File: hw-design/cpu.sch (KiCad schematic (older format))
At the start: 15 parts, among them P2 HEADER_5X2, P3 HEADER_5X2, U1 LPC1113FBD48/302, X1 10MHz

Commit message: ERC passing
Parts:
- removed P2, P3: HEADER_5X2, MOD_Footprints_Lib:PIN_ARRAY_5x2, symbol CONN_5X2
- added P1, P2: CONN_02X05, symbol CONN_02X05
- renumbered C10 to C13, C11 to C14, C14 to C15, C13 to C16, R21 to R23, R15 to R24, R29 to R25, R30 to R26, R26 to R27, R27 to R28, U1 to U4
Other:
- moved on the sheet: R27, R28

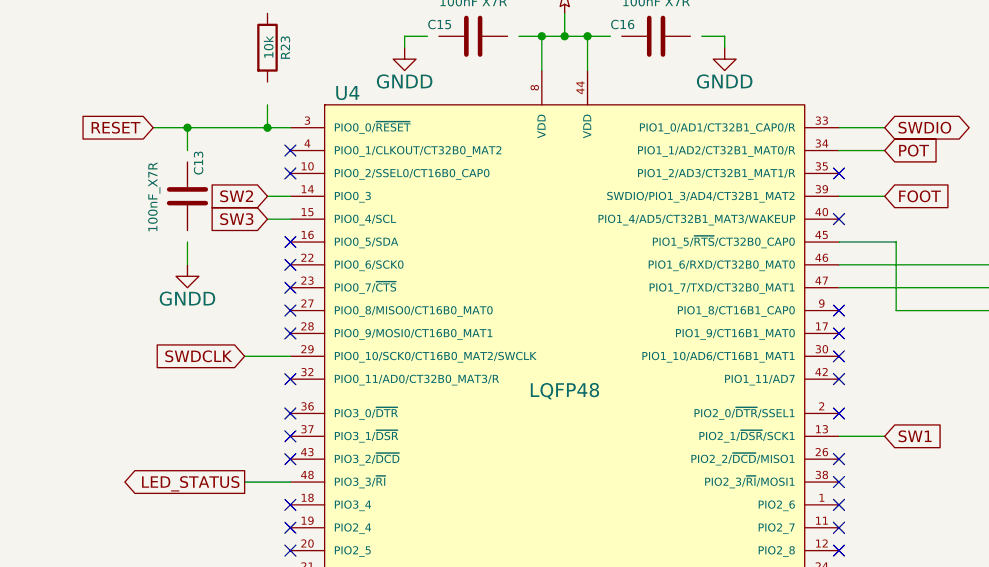
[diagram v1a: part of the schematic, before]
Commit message: wip: footprint association using default kicad libraries
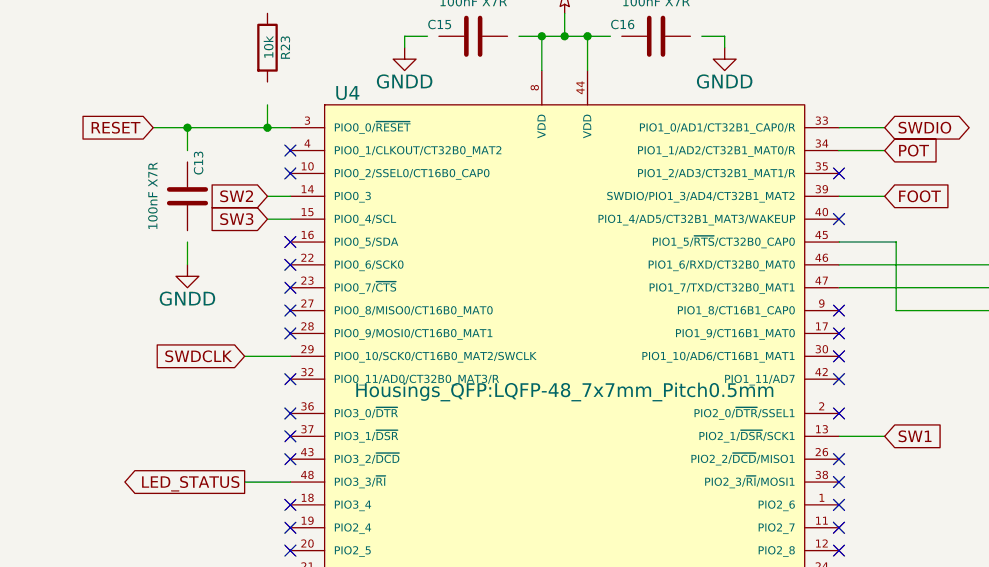
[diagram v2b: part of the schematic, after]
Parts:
- C12, C14, C15, C16: footprint MOD_Footprints_Lib:SM0603 -> Capacitors_SMD:C_0603
- C13: value 100nF_X7R -> 100nF X7R; footprint MOD_Footprints_Lib:SM0603 -> Capacitors_SMD:C_0603
- P1, P2: footprint (none) -> Pin_Headers:Pin_Header_Straight_2x05
- R23, R24, R25, R26, R27, R28: footprint MOD_Footprints_Lib:SM0603 -> Resistors_SMD:R_0603
- U4: footprint LQFP48 -> Housings_QFP:LQFP-48_7x7mm_Pitch0.5mm
- X1: footprint MOD_Footprints_Lib:HC_49US -> Crystals_Oscillators_SMD:Q_49U3HMS
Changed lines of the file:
@@
 F 0 "C15" V 4000 1750 40  0000 L CNN
 F 1 "100nF X7R" V 3900 1800 40  0000 L CNN
-F 2 "MOD_Footprints_Lib:SM0603" H 4088 1800 30  0001 C CNN
+F 2 "Capacitors_SMD:C_0603" H 4088 1800 30  0001 C CNN
 F 3 "~" H 4050 1950 60  0000 C CNN
 	1    4050 1950
@@
 F 0 "C16" V 4900 1750 40  0000 L CNN
 F 1 "100nF X7R" V 5000 1800 40  0000 L CNN
-F 2 "MOD_Footprints_Lib:SM0603" H 4888 1800 30  0001 C CNN
+F 2 "Capacitors_SMD:C_0603" H 4888 1800 30  0001 C CNN
 F 3 "~" H 4850 1950 60  0000 C CNN
 	1    4850 1950
@@
 F 0 "X1" H 2700 4800 60  0000 C CNN
 F 1 "10MHz" H 2700 4550 60  0000 C CNN
-F 2 "MOD_Footprints_Lib:HC_49US" H 2700 4700 60  0001 C CNN
+F 2 "Crystals_Oscillators_SMD:Q_49U3HMS" H 2700 4700 60  0001 C CNN
 F 3 "~" H 2700 4700 60  0000 C CNN
 	1    2700 4700
@@
 F 0 "C14" V 2950 5000 40  0000 L CNN
 F 1 "18pF X7R" V 3250 4900 40  0000 L CNN
-F 2 "MOD_Footprints_Lib:SM0603" H 3138 4900 30  0001 C CNN
+F 2 "Capacitors_SMD:C_0603" H 3138 4900 30  0001 C CNN
 F 3 "~" H 3100 5050 60  0000 C CNN
 	1    3100 5050
@@
 F 0 "C12" V 2100 5000 40  0000 L CNN
 F 1 "18pF X7R" V 2400 4900 40  0000 L CNN
-F 2 "MOD_Footprints_Lib:SM0603" H 2288 4900 30  0001 C CNN
+F 2 "Capacitors_SMD:C_0603" H 2288 4900 30  0001 C CNN
 F 3 "~" H 2250 5050 60  0000 C CNN
 	1    2250 5050
@@
 F 0 "R23" V 3230 2000 40  0000 C CNN
 F 1 "10k" V 3157 2001 40  0000 C CNN
-F 2 "MOD_Footprints_Lib:SM0603" V 3080 2000 30  0001 C CNN
+F 2 "Resistors_SMD:R_0603" V 3080 2000 30  0001 C CNN
 F 3 "~" H 3150 2000 30  0000 C CNN
 	1    3150 2000
@@
 P 2800 2650
 F 0 "C13" V 2850 2450 40  0000 L CNN
-F 1 "100nF_X7R" V 2650 2500 40  0000 L CNN
-F 2 "MOD_Footprints_Lib:SM0603" H 2838 2500 30  0001 C CNN
+F 1 "100nF X7R" V 2650 2500 40  0000 L CNN
+F 2 "Capacitors_SMD:C_0603" H 2838 2500 30  0001 C CNN
 F 3 "~" H 2800 2650 60  0000 C CNN
 	1    2800 2650
@@
 F 0 "R28" V 9100 4850 40  0000 C CNN
 F 1 "100R" V 9007 4851 40  0000 C CNN
-F 2 "MOD_Footprints_Lib:SM0603" V 8930 4850 30  0001 C CNN
+F 2 "Resistors_SMD:R_0603" V 8930 4850 30  0001 C CNN
 F 3 "~" H 9000 4850 30  0000 C CNN
 	1    9000 4850
@@
 F 0 "R27" V 8900 4750 40  0000 C CNN
 F 1 "100R" V 9007 4751 40  0000 C CNN
-F 2 "MOD_Footprints_Lib:SM0603" V 8930 4750 30  0001 C CNN
+F 2 "Resistors_SMD:R_0603" V 8930 4750 30  0001 C CNN
 F 3 "~" H 9000 4750 30  0000 C CNN
 	1    9000 4750
@@
 F 0 "U4" H 3500 4800 60  0000 C CNN
 F 1 "LPC1113FBD48/302" H 5100 2150 60  0000 C CNN
-F 2 "LQFP48" H 4450 3500 60  0000 C CNN
+F 2 "Housings_QFP:LQFP-48_7x7mm_Pitch0.5mm" H 4450 3500 60  0000 C CNN
 F 3 "" H 4450 3500 60  0000 C CNN
 	1    4450 3500
@@
 F 0 "R24" V 7180 3450 40  0000 C CNN
 F 1 "0R" V 7107 3451 40  0000 C CNN
-F 2 "MOD_Footprints_Lib:SM0603" V 7030 3450 30  0001 C CNN
+F 2 "Resistors_SMD:R_0603" V 7030 3450 30  0001 C CNN
 F 3 "~" H 7100 3450 30  0000 C CNN
 	1    7100 3450
@@
 F 0 "R25" V 7180 3650 40  0000 C CNN
 F 1 "0R" V 7107 3651 40  0000 C CNN
-F 2 "MOD_Footprints_Lib:SM0603" V 7030 3650 30  0001 C CNN
+F 2 "Resistors_SMD:R_0603" V 7030 3650 30  0001 C CNN
 F 3 "~" H 7100 3650 30  0000 C CNN
 	1    7100 3650
@@
 F 0 "R26" V 7180 3850 40  0000 C CNN
 F 1 "0R" V 7107 3851 40  0000 C CNN
-F 2 "MOD_Footprints_Lib:SM0603" V 7030 3850 30  0001 C CNN
+F 2 "Resistors_SMD:R_0603" V 7030 3850 30  0001 C CNN
 F 3 "~" H 7100 3850 30  0000 C CNN
 	1    7100 3850
@@
 F 0 "P1" H 7100 3250 50  0000 C CNN
 F 1 "CONN_02X05" H 7100 2650 50  0000 C CNN
-F 2 "" H 7100 1750 60  0000 C CNN
+F 2 "Pin_Headers:Pin_Header_Straight_2x05" H 7100 1750 60  0001 C CNN
 F 3 "" H 7100 1750 60  0000 C CNN
 	1    7100 2950
@@
 F 0 "P2" H 8400 5250 50  0000 C CNN
 F 1 "CONN_02X05" H 8400 4650 50  0000 C CNN
-F 2 "" H 8400 3750 60  0000 C CNN
+F 2 "Pin_Headers:Pin_Header_Straight_2x05" H 8400 3750 60  0001 C CNN
 F 3 "" H 8400 3750 60  0000 C CNN
 	1    8400 4950

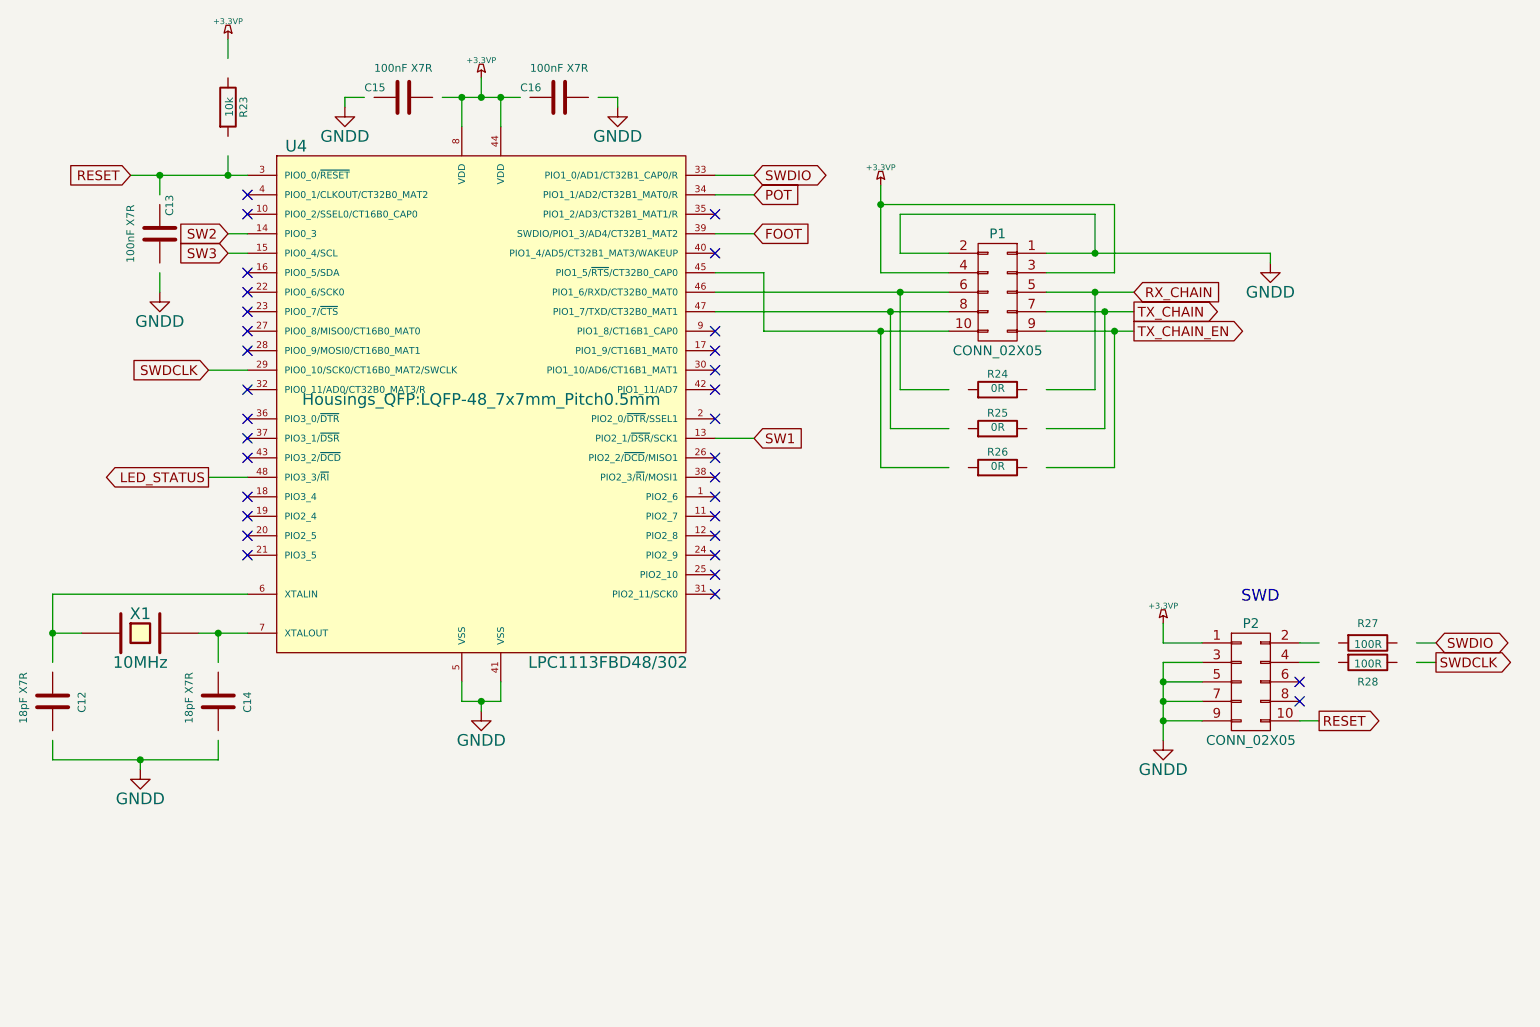
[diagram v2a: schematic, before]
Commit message: adding official kicad library as submodule
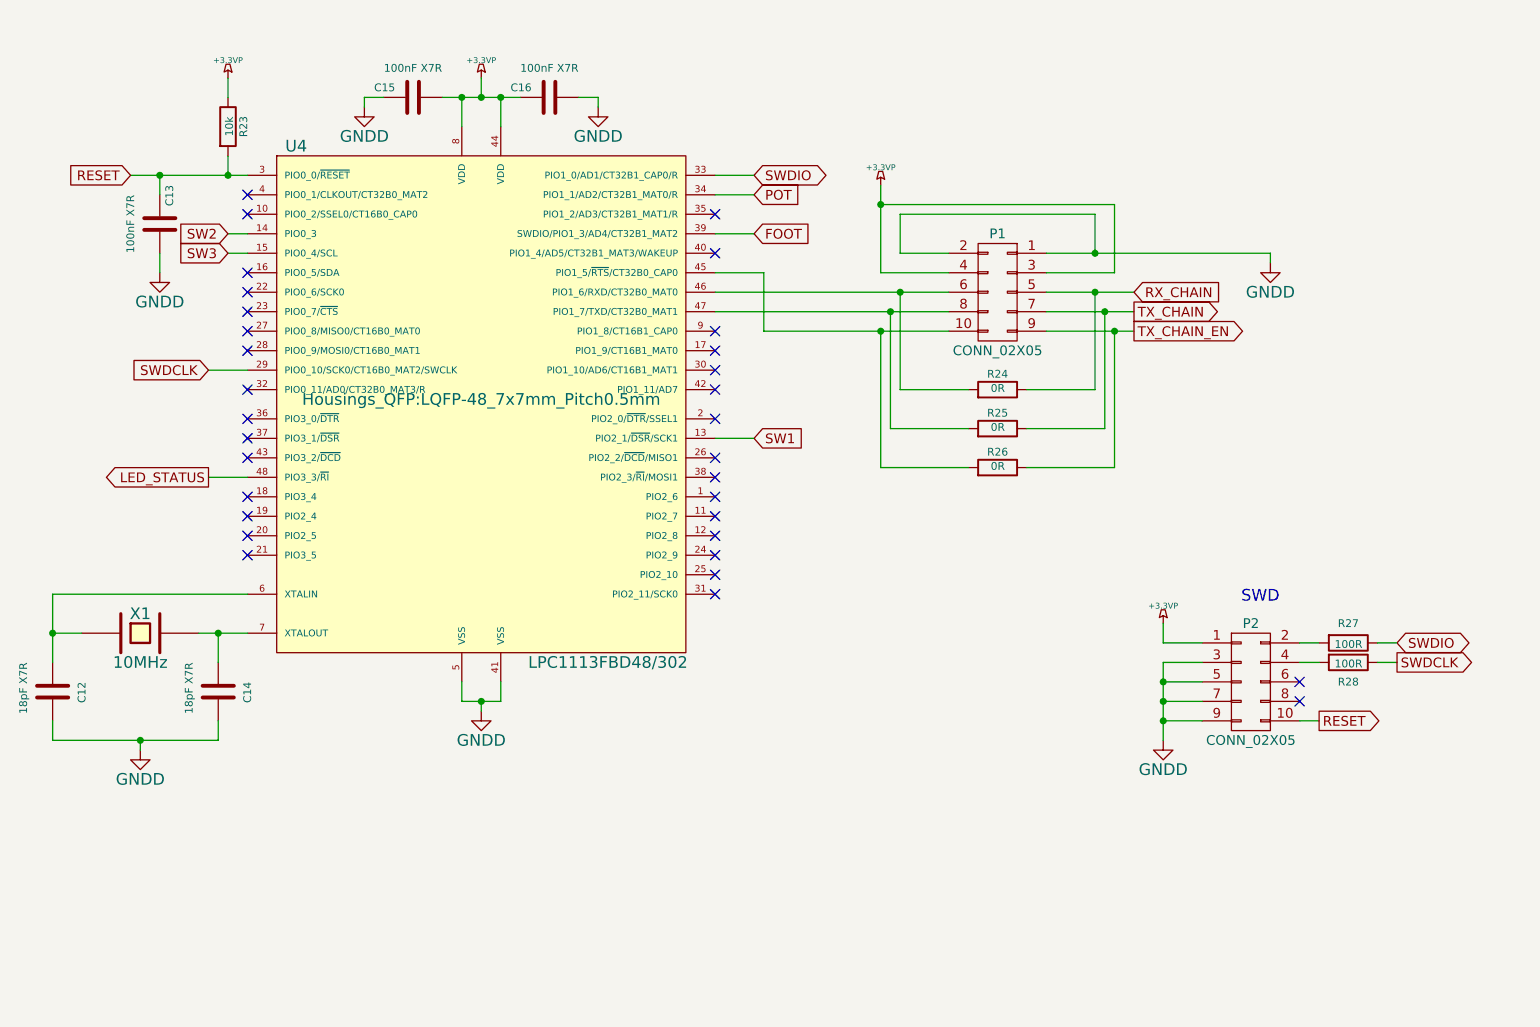
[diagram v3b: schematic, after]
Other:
- moved on the sheet: C12, C13, C14, C15, C16, R23, R27, R28
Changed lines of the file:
@@
 L C C15
 U 1 1 548B6D77
-P 4050 1950
-F 0 "C15" V 4000 1750 40  0000 L CNN
-F 1 "100nF X7R" V 3900 1800 40  0000 L CNN
-F 2 "Capacitors_SMD:C_0603" H 4088 1800 30  0001 C CNN
-F 3 "~" H 4050 1950 60  0000 C CNN
-	1    4050 1950
+P 4100 1950
+F 0 "C15" V 4050 1750 40  0000 L CNN
+F 1 "100nF X7R" V 3950 1800 40  0000 L CNN
+F 2 "Capacitors_SMD:C_0603" H 4138 1800 30  0001 C CNN
+F 3 "~" H 4100 1950 60  0000 C CNN
+	1    4100 1950
 	0    1    1    0
 $EndComp
@@
 L C C16
 U 1 1 548B6D84
-P 4850 1950
-F 0 "C16" V 4900 1750 40  0000 L CNN
-F 1 "100nF X7R" V 5000 1800 40  0000 L CNN
-F 2 "Capacitors_SMD:C_0603" H 4888 1800 30  0001 C CNN
-F 3 "~" H 4850 1950 60  0000 C CNN
-	1    4850 1950
+P 4800 1950
+F 0 "C16" V 4850 1750 40  0000 L CNN
+F 1 "100nF X7R" V 4950 1800 40  0000 L CNN
+F 2 "Capacitors_SMD:C_0603" H 4838 1800 30  0001 C CNN
+F 3 "~" H 4800 1950 60  0000 C CNN
+	1    4800 1950
 	0    1    -1   0
 $EndComp
@@
 L C C14
 U 1 1 548B6DA4
-P 3100 5050
-F 0 "C14" V 2950 5000 40  0000 L CNN
-F 1 "18pF X7R" V 3250 4900 40  0000 L CNN
-F 2 "Capacitors_SMD:C_0603" H 3138 4900 30  0001 C CNN
-F 3 "~" H 3100 5050 60  0000 C CNN
-	1    3100 5050
+P 3100 5000
+F 0 "C14" V 2950 4950 40  0000 L CNN
+F 1 "18pF X7R" V 3250 4850 40  0000 L CNN
+F 2 "Capacitors_SMD:C_0603" H 3138 4850 30  0001 C CNN
+F 3 "~" H 3100 5000 60  0000 C CNN
+	1    3100 5000
 	-1   0    0    1
 $EndComp
@@
 L C C12
 U 1 1 548B6DB7
-P 2250 5050
-F 0 "C12" V 2100 5000 40  0000 L CNN
-F 1 "18pF X7R" V 2400 4900 40  0000 L CNN
-F 2 "Capacitors_SMD:C_0603" H 2288 4900 30  0001 C CNN
-F 3 "~" H 2250 5050 60  0000 C CNN
-	1    2250 5050
+P 2250 5000
+F 0 "C12" V 2100 4950 40  0000 L CNN
+F 1 "18pF X7R" V 2400 4850 40  0000 L CNN
+F 2 "Capacitors_SMD:C_0603" H 2288 4850 30  0001 C CNN
+F 3 "~" H 2250 5000 60  0000 C CNN
+	1    2250 5000
 	-1   0    0    1
 $EndComp
@@
 L R R23
 U 1 1 548B6DBE
-P 3150 2000
-F 0 "R23" V 3230 2000 40  0000 C CNN
-F 1 "10k" V 3157 2001 40  0000 C CNN
-F 2 "Resistors_SMD:R_0603" V 3080 2000 30  0001 C CNN
-F 3 "~" H 3150 2000 30  0000 C CNN
-	1    3150 2000
+P 3150 2100
+F 0 "R23" V 3230 2100 40  0000 C CNN
+F 1 "10k" V 3157 2101 40  0000 C CNN
+F 2 "Resistors_SMD:R_0603" V 3080 2100 30  0001 C CNN
+F 3 "~" H 3150 2100 30  0000 C CNN
+	1    3150 2100
 	1    0    0    -1
 $EndComp
@@
 L C C13
 U 1 1 548B6DC5
-P 2800 2650
-F 0 "C13" V 2850 2450 40  0000 L CNN
-F 1 "100nF X7R" V 2650 2500 40  0000 L CNN
-F 2 "Capacitors_SMD:C_0603" H 2838 2500 30  0001 C CNN
-F 3 "~" H 2800 2650 60  0000 C CNN
-	1    2800 2650
+P 2800 2600
+F 0 "C13" V 2850 2400 40  0000 L CNN
+F 1 "100nF X7R" V 2650 2450 40  0000 L CNN
+F 2 "Capacitors_SMD:C_0603" H 2838 2450 30  0001 C CNN
+F 3 "~" H 2800 2600 60  0000 C CNN
+	1    2800 2600
 	1    0    0    1
 $EndComp
-Text GLabel 9350 4750 2    50   BiDi ~ 0
+Text GLabel 9150 4750 2    50   BiDi ~ 0
 SWDIO
-Text GLabel 9350 4850 2    50   Output ~ 0
+Text GLabel 9150 4850 2    50   Output ~ 0
 SWDCLK
 Text GLabel 5850 2350 2    50   BiDi ~ 0
@@
 L R R28
 U 1 1 548B6E40
-P 9000 4850
-F 0 "R28" V 9100 4850 40  0000 C CNN
-F 1 "100R" V 9007 4851 40  0000 C CNN
-F 2 "Resistors_SMD:R_0603" V 8930 4850 30  0001 C CNN
-F 3 "~" H 9000 4850 30  0000 C CNN
-	1    9000 4850
+P 8900 4850
+F 0 "R28" V 9000 4850 40  0000 C CNN
+F 1 "100R" V 8907 4851 40  0000 C CNN
+F 2 "Resistors_SMD:R_0603" V 8830 4850 30  0001 C CNN
+F 3 "~" H 8900 4850 30  0000 C CNN
+	1    8900 4850
 	0    1    1    0
 $EndComp
@@
 L R R27
 U 1 1 548B6E47
-P 9000 4750
-F 0 "R27" V 8900 4750 40  0000 C CNN
-F 1 "100R" V 9007 4751 40  0000 C CNN
-F 2 "Resistors_SMD:R_0603" V 8930 4750 30  0001 C CNN
-F 3 "~" H 9000 4750 30  0000 C CNN
-	1    9000 4750
+P 8900 4750
+F 0 "R27" V 8800 4750 40  0000 C CNN
+F 1 "100R" V 8907 4751 40  0000 C CNN
+F 2 "Resistors_SMD:R_0603" V 8830 4750 30  0001 C CNN
+F 3 "~" H 8900 4750 30  0000 C CNN
+	1    8900 4750
 	0    1    1    0
 $EndComp
@@
 L GNDD #PWR050
 U 1 1 54E37CE9
-P 2700 5400
-F 0 "#PWR050" H 2700 5150 60  0001 C CNN
-F 1 "GNDD" H 2700 5250 60  0000 C CNN
-F 2 "" H 2700 5400 60  0000 C CNN
-F 3 "" H 2700 5400 60  0000 C CNN
-	1    2700 5400
+P 2700 5300
+F 0 "#PWR050" H 2700 5050 60  0001 C CNN
+F 1 "GNDD" H 2700 5150 60  0000 C CNN
+F 2 "" H 2700 5300 60  0000 C CNN
+F 3 "" H 2700 5300 60  0000 C CNN
+	1    2700 5300
 	1    0    0    -1
 $EndComp
@@
 L GNDD #PWR051
 U 1 1 54E3D56C
-P 3750 2000
-F 0 "#PWR051" H 3750 1750 60  0001 C CNN
-F 1 "GNDD" H 3750 1850 60  0000 C CNN
-F 2 "" H 3750 2000 60  0000 C CNN
-F 3 "" H 3750 2000 60  0000 C CNN
-	1    3750 2000
+P 3850 2000
+F 0 "#PWR051" H 3850 1750 60  0001 C CNN
+F 1 "GNDD" H 3850 1850 60  0000 C CNN
+F 2 "" H 3850 2000 60  0000 C CNN
+F 3 "" H 3850 2000 60  0000 C CNN
+	1    3850 2000
 	1    0    0    -1
 $EndComp
@@
 L GNDD #PWR052
 U 1 1 54E3D638
-P 5150 2000
-F 0 "#PWR052" H 5150 1750 60  0001 C CNN
-F 1 "GNDD" H 5150 1850 60  0000 C CNN
-F 2 "" H 5150 2000 60  0000 C CNN
-F 3 "" H 5150 2000 60  0000 C CNN
-	1    5150 2000
+P 5050 2000
+F 0 "#PWR052" H 5050 1750 60  0001 C CNN
+F 1 "GNDD" H 5050 1850 60  0000 C CNN
+F 2 "" H 5050 2000 60  0000 C CNN
+F 3 "" H 5050 2000 60  0000 C CNN
+	1    5050 2000
 	1    0    0    -1
 $EndComp
@@
 L GNDD #PWR056
 U 1 1 54E52BA2
-P 2800 2950
-F 0 "#PWR056" H 2800 2700 60  0001 C CNN
-F 1 "GNDD" H 2800 2800 60  0000 C CNN
-F 2 "" H 2800 2950 60  0000 C CNN
-F 3 "" H 2800 2950 60  0000 C CNN
-	1    2800 2950
+P 2800 2850
+F 0 "#PWR056" H 2800 2600 60  0001 C CNN
+F 1 "GNDD" H 2800 2700 60  0000 C CNN
+F 2 "" H 2800 2850 60  0000 C CNN
+F 3 "" H 2800 2850 60  0000 C CNN
+	1    2800 2850
 	1    0    0    -1
 $EndComp
@@
 L +3.3VP #PWR057
 U 1 1 54E5359B
-P 3150 1650
-F 0 "#PWR057" H 3200 1680 20  0001 C CNN
-F 1 "+3.3VP" H 3150 1740 30  0000 C CNN
-F 2 "" H 3150 1650 60  0000 C CNN
-F 3 "" H 3150 1650 60  0000 C CNN
-	1    3150 1650
+P 3150 1850
+F 0 "#PWR057" H 3200 1880 20  0001 C CNN
+F 1 "+3.3VP" H 3150 1940 30  0000 C CNN
+F 2 "" H 3150 1850 60  0000 C CNN
+F 3 "" H 3150 1850 60  0000 C CNN
+	1    3150 1850
 	1    0    0    -1
 $EndComp
@@
 	7950 4850 8150 4850
 Wire Wire Line
-	9250 4750 9350 4750
-Wire Wire Line
-	9350 4850 9250 4850
+	9050 4750 9150 4750
+Wire Wire Line
+	9150 4850 9050 4850
 Wire Wire Line
 	5850 2350 5650 2350
@@
 Connection ~ 4450 5050
 Wire Wire Line
-	2250 5250 2250 5350
-Wire Wire Line
-	2250 5350 3100 5350
-Wire Wire Line
-	3100 5350 3100 5250
-Wire Wire Line
-	2700 5400 2700 5350
-Connection ~ 2700 5350
-Wire Wire Line
-	3750 2000 3750 1950
-Wire Wire Line
-	3750 1950 3850 1950
-Wire Wire Line
-	5050 1950 5150 1950
-Wire Wire Line
-	5150 1950 5150 2000
+	2250 5150 2250 5250
+Wire Wire Line
+	2250 5250 3100 5250
+Wire Wire Line
+	3100 5250 3100 5150
+Wire Wire Line
+	2700 5300 2700 5250
+Connection ~ 2700 5250
+Wire Wire Line
+	3850 2000 3850 1950
+Wire Wire Line
+	3850 1950 3950 1950
+Wire Wire Line
+	4950 1950 5050 1950
+Wire Wire Line
+	5050 1950 5050 2000
 Wire Wire Line
 	4250 1950 4650 1950
@@
 	8500 2750 8500 2800
 Wire Wire Line
-	6600 3450 6850 3450
-Wire Wire Line
-	7600 3450 7350 3450
+	6600 3450 6950 3450
+Wire Wire Line
+	7600 3450 7250 3450
 Wire Wire Line
 	6600 3450 6600 2950
@@
 	7600 3450 7600 2950
 Wire Wire Line
-	6550 3650 6850 3650
-Wire Wire Line
-	7650 3650 7350 3650
-Wire Wire Line
-	6500 3850 6850 3850
+	6550 3650 6950 3650
+Wire Wire Line
+	7650 3650 7250 3650
+Wire Wire Line
+	6500 3850 6950 3850
 Wire Wire Line
 	6550 3650 6550 3050
@@
 	7700 3150 7700 3850
 Wire Wire Line
-	7700 3850 7350 3850
+	7700 3850 7250 3850
 Wire Wire Line
 	6500 3850 6500 3150
@@
 Connection ~ 6500 2500
 Wire Wire Line
-	2800 2850 2800 2950
-Wire Wire Line
-	3150 1750 3150 1650
+	2800 2750 2800 2850
+Wire Wire Line
+	3150 1950 3150 1850
 Wire Wire Line
 	7950 4750 8150 4750
